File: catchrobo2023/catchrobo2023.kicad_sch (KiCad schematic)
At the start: 35 parts, among them J1 Conn_01x02_Male, J2 Conn_01x02_Male, J3 Conn_01x02_Male, J4 Conn_01x02_Male, J5 Conn_01x02_Male, J6 Conn_01x02_Male, J7 Conn_01x03_Male, J8 Conn_01x03_Male, J9 Conn_01x03_Male, Q1 AO3401A, SW1 SW_SPDT, SW2 SW_DIP_x04, U1 RaspberryPiPicoW, U2 AZ1084-5.0, U3 LBR-127HLD, U4 LBR-127HLD, U5 LBR-127HLD, U6 LBR-127HLD, U7 CD4051BM96, U8 SPT15

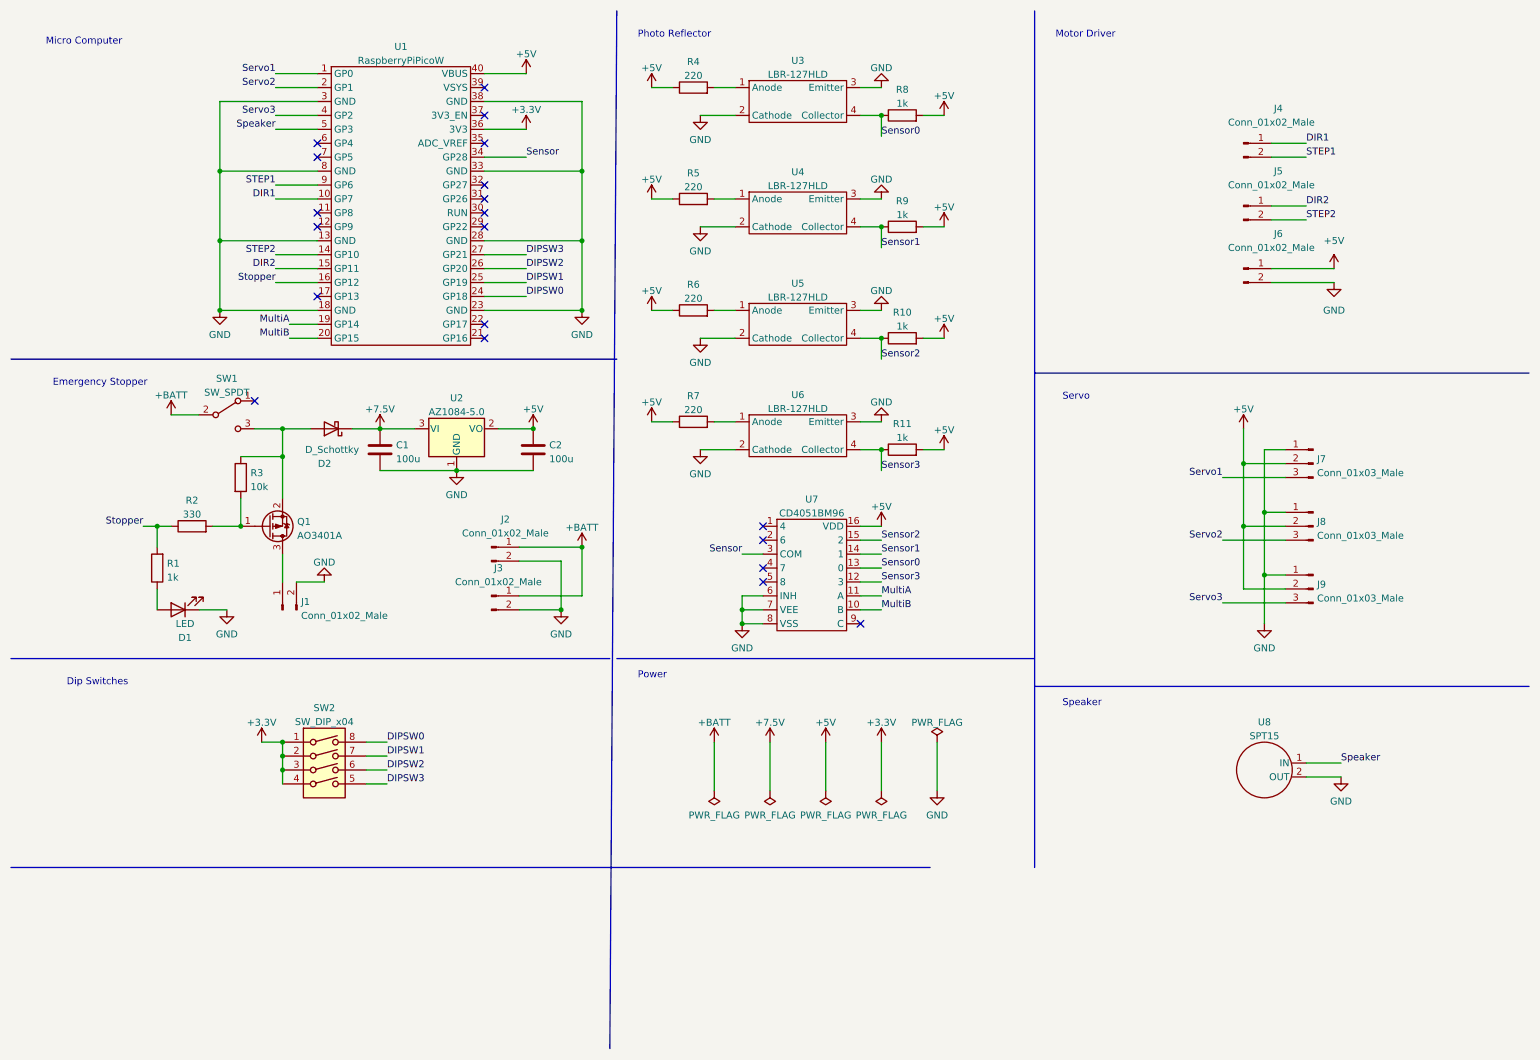
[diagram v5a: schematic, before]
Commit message: コントローラへの配線以外は完了
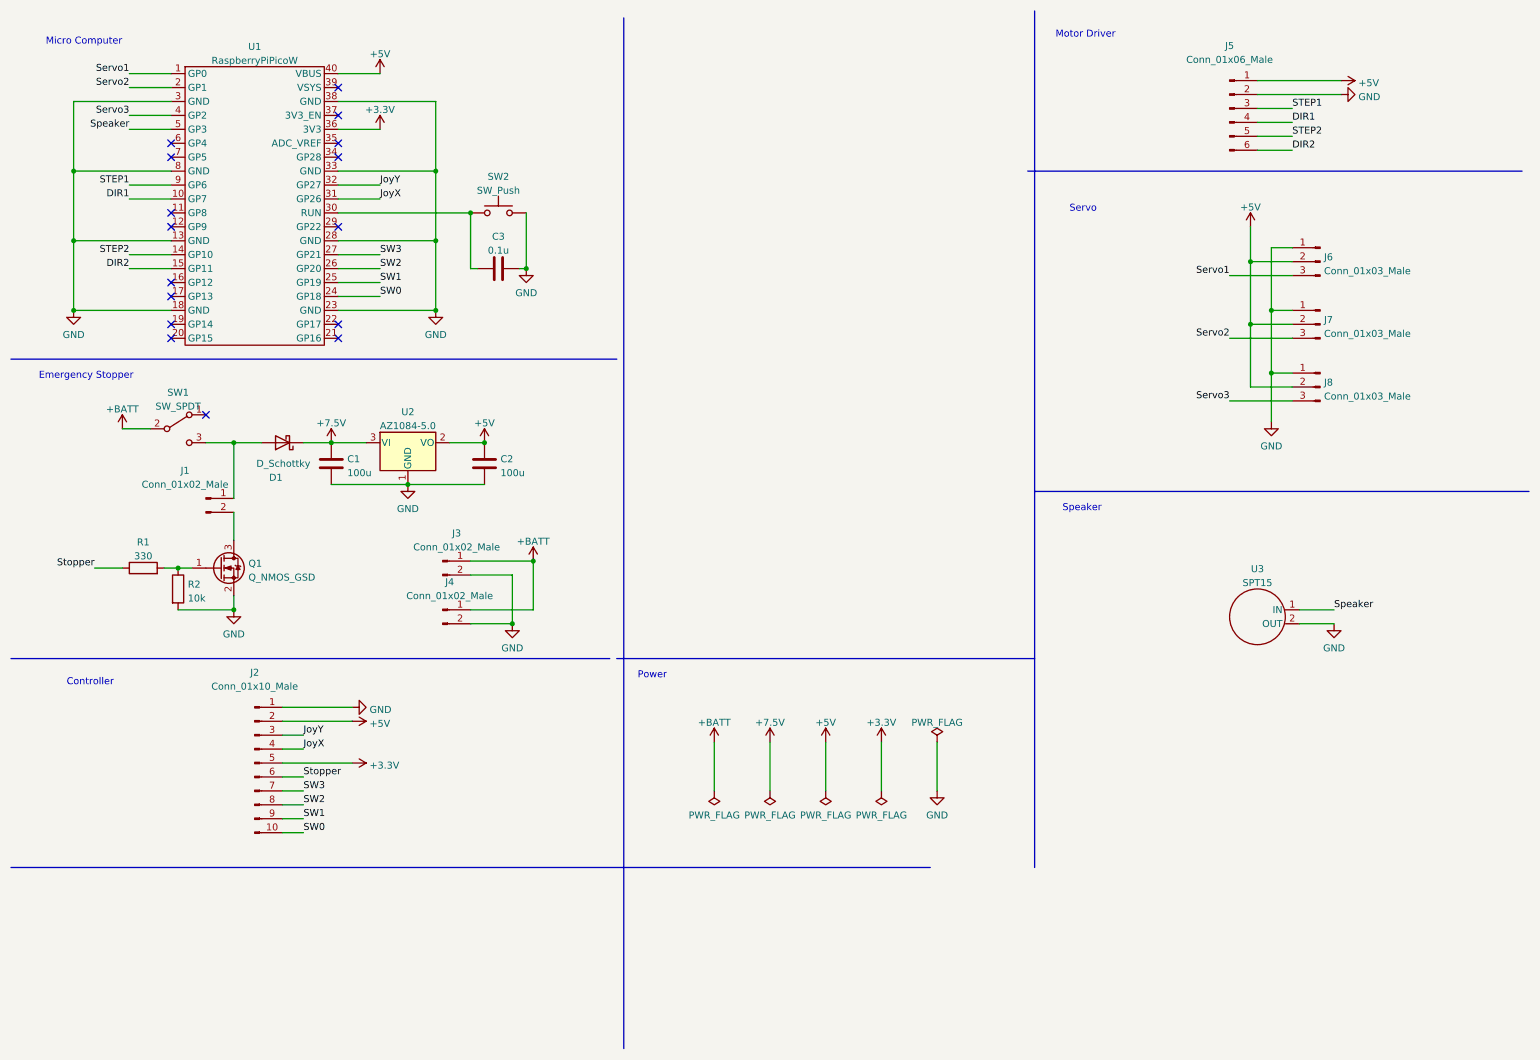
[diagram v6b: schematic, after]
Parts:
- removed D1: LED, LED_THT:LED_D5.0mm, symbol Device:LED
- removed J4, J5, J6: Conn_01x02_Male, Connector_JST:JST_XH_B2B-XH-AM_1x02_P2.50mm_Vertical, symbol Connector:Conn_01x02_Male
- removed Q1: AO3401A, Package_TO_SOT_SMD:SOT-23, symbol Transistor_FET:AO3401A
- removed R10, R11, R8, R9: 1k, Resistor_SMD:R_0402_1005Metric, symbol Device:R
- removed R3: 10k, Resistor_SMD:R_0603_1608Metric, symbol Device:R
- removed R4, R5, R6, R7: 220, Resistor_SMD:R_0603_1608Metric, symbol Device:R
- removed SW2: SW_DIP_x04, Package_DIP:DIP-8_W7.62mm, symbol Switch:SW_DIP_x04
- removed U3, U4, U5, U6: LBR-127HLD, Connector_PinHeader_2.54mm:PinHeader_1x04_P2.54mm_Vertical, symbol catchrobo_parts:LBR-127HLD
- removed U7: CD4051BM96, Catchrobo_parts:SOIC-16-150mil, symbol catchrobo_parts:CD4051BM96
- added C3: 0.1u, Capacitor_SMD:C_0603_1608Metric, symbol Device:C
- added J2: Conn_01x10_Male, Connector_JST:JST_XH_S10B-XH-A_1x10_P2.50mm_Horizontal, symbol Connector:Conn_01x10_Male
- added J5: Conn_01x06_Male, Connector_JST:JST_XH_S6B-XH-A_1x06_P2.50mm_Horizontal, symbol Connector:Conn_01x06_Male
- added Q1: Q_NMOS_GSD, Package_TO_SOT_SMD:SOT-23, symbol Device:Q_NMOS_GSD
- added SW2: SW_Push, Catchrobo_parts:TactSwitch, symbol Switch:SW_Push
- J3: renamed from J2; footprint Connector_JST:JST_XH_B2B-XH-AM_1x02_P2.50mm_Vertical -> Connector_JST:JST_XH_S2B-XH-A_1x02_P2.50mm_Horizontal
- J4: renamed from J3; footprint Connector_JST:JST_XH_B2B-XH-AM_1x02_P2.50mm_Vertical -> Connector_JST:JST_XH_S2B-XH-A_1x02_P2.50mm_Horizontal
- R1: value 1k -> 330; footprint Resistor_SMD:R_0402_1005Metric -> Resistor_SMD:R_0603_1608Metric; LCSC (none) -> C23138
- R2: value 330 -> 10k; LCSC C23138 -> C25804
- U3: renamed from U8; footprint Connector_JST:JST_XH_B2B-XH-AM_1x02_P2.50mm_Vertical -> Catchrobo_parts:PKM13EPYH4000-A0
- renumbered D2 to D1, J7 to J6, J8 to J7, J9 to J8
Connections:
- net +3.3V: now also J2.5 (Pin_5)
- net +5V: now also J2.2 (Pin_2), J5.1 (Pin_1)
- net DIR1: now also J5.4 (Pin_4)
- net DIR2: now also J5.6 (Pin_6)
- net GND: now also R2.2, C3.2, J2.1 (Pin_1), J5.2 (Pin_2), Q1.2 (S), SW2.2; no longer J1.2 (Pin_2)
- net STEP1: now also J5.3 (Pin_3)
- net STEP2: now also J5.5 (Pin_5)
- net Stopper: now also R1.1, J2.6 (Pin_6); no longer R1.2, R2.1, U1.16 (GP12)
- net at J1.1 (Pin_1): now also D1.2 (A), SW1.3 (C)
- net at U1.30 (RUN): now also C3.1, SW2.1
- net JoyX: now reaches U1.31 (GP26)
- net JoyX: now also J2.4 (Pin_4)
- net JoyY: now reaches U1.32 (GP27)
- net JoyY: now also J2.3 (Pin_3)
- net DIPSW0 renamed SW0
- net SW0: now also J2.10 (Pin_10)
- net DIPSW1 renamed SW1
- net SW1: now also J2.9 (Pin_9)
- net DIPSW2 renamed SW2
- net SW2: now also J2.8 (Pin_8)
- net DIPSW3 renamed SW3
- net SW3: now also J2.7 (Pin_7)
- net MultiA: no longer names the net of U1.19 (GP14)
- net MultiB: no longer names the net of U1.20 (GP15)
- net Sensor: no longer names the net of U1.34 (GP28)
- new net: Q1.1 (G), R1.2, R2.1
- new net: J1.2 (Pin_2), Q1.3 (D)
- no-connect marks 20 -> 16
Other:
- note added: "Controller"
- note removed: "Dip Switches"
- note removed: "Photo Reflector"
- moved on the sheet: C1, C2, D1, J1, J3, J4, J6, J7, J8, SW1, U1, U2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

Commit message: pchFetによる電源スイッチを追加
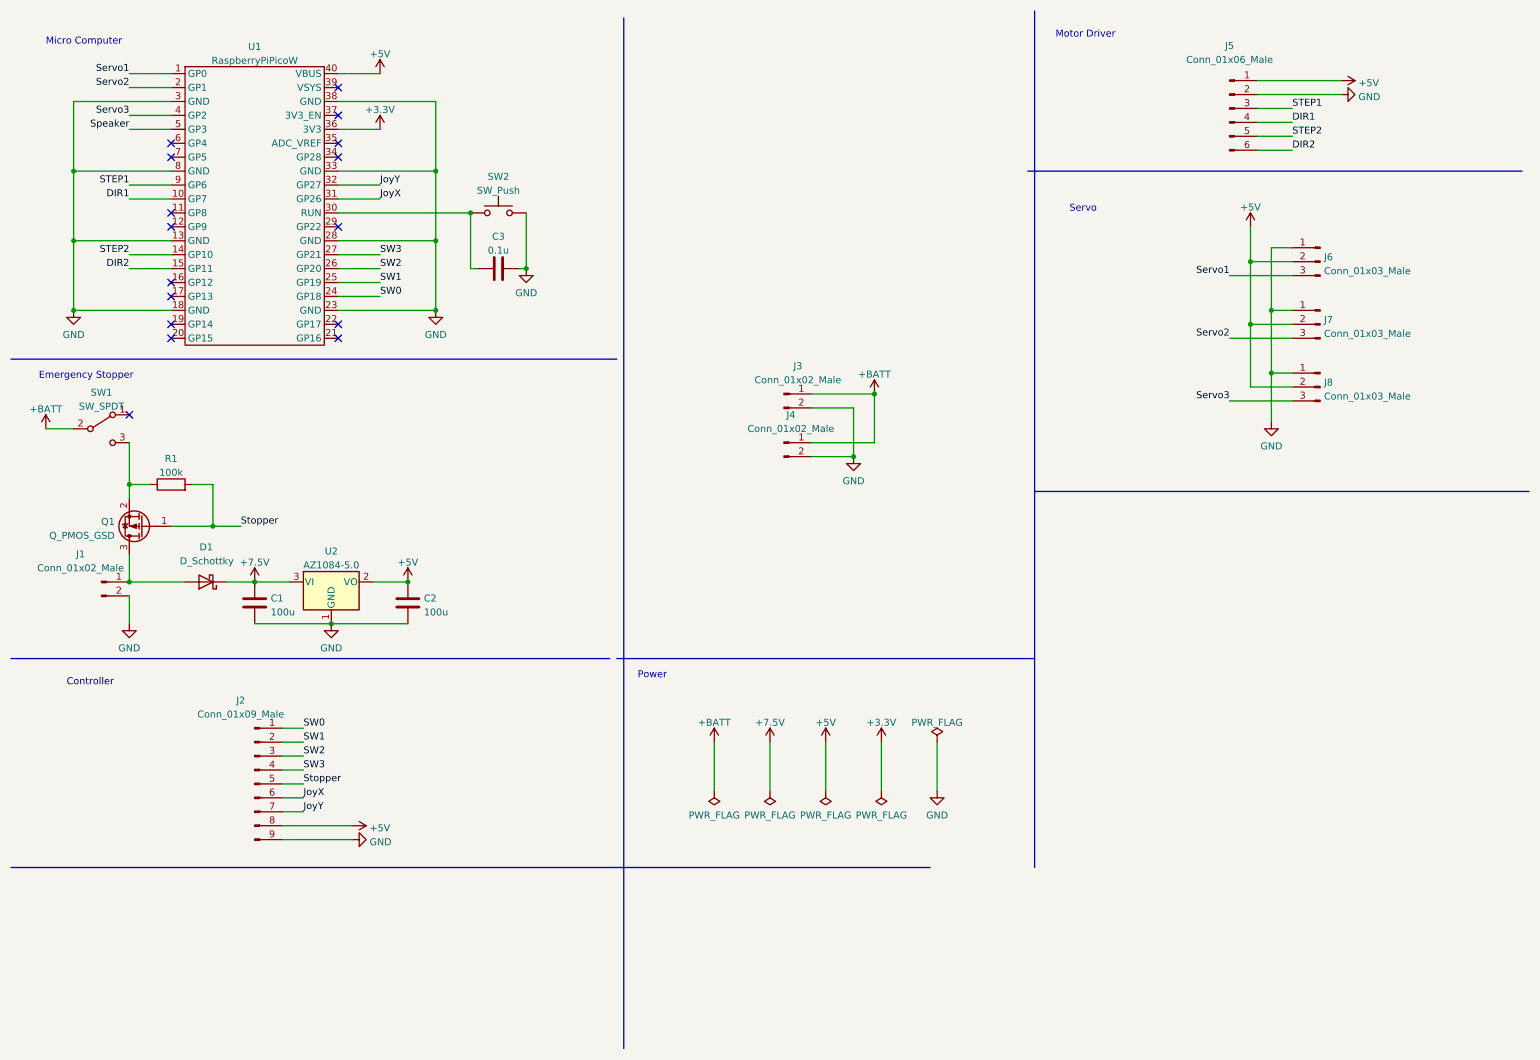
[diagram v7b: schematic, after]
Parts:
- removed J2: Conn_01x10_Male, Connector_JST:JST_XH_S10B-XH-A_1x10_P2.50mm_Horizontal, symbol Connector:Conn_01x10_Male
- removed Q1: Q_NMOS_GSD, Package_TO_SOT_SMD:SOT-23, symbol Device:Q_NMOS_GSD
- removed R2: 10k, Resistor_SMD:R_0603_1608Metric, symbol Device:R
- removed U3: SPT15, Catchrobo_parts:PKM13EPYH4000-A0, symbol catchrobo_parts:SPT15
- added J2: Conn_01x09_Male, Connector_JST:JST_XH_S9B-XH-A-1_1x09_P2.50mm_Horizontal, symbol Connector:Conn_01x09_Male
- added Q1: Q_PMOS_GSD, Package_TO_SOT_SMD:SOT-23, symbol Device:Q_PMOS_GSD
- J1: footprint Connector_JST:JST_XH_B2B-XH-AM_1x02_P2.50mm_Vertical -> Connector_JST:JST_XH_B2B-XH-A_1x02_P2.50mm_Vertical
- R1: value 330 -> 100k; LCSC C23138 -> C25803
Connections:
- net +5V: now also J2.8 (Pin_8)
- net GND: now also J1.2 (Pin_2), J2.9 (Pin_9)
- net JoyX: now also J2.6 (Pin_6)
- net JoyY: now also J2.7 (Pin_7)
- net SW0: now also J2.1 (Pin_1)
- net SW1: now also J2.2 (Pin_2)
- net SW2: now also J2.3 (Pin_3)
- net SW3: now also J2.4 (Pin_4)
- net Stopper: now also R1.2, J2.5 (Pin_5), Q1.1 (G); no longer R1.1
- net at D1.2 (A), J1.1 (Pin_1): now also Q1.3 (D); no longer SW1.3 (C)
- new net: Q1.2 (S), R1.1, SW1.3 (C)
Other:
- note removed: "Speaker"
- moved on the sheet: C1, C2, D1, J1, J3, J4, SW1, U2

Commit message: 回収機基板設計完了
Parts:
- removed SW1: SW_SPDT, Catchrobo_parts:2MS1-T1-B4-M2-Q-E-S, symbol Switch:SW_SPDT
- J1: footprint Connector_JST:JST_XH_B2B-XH-A_1x02_P2.50mm_Vertical -> Connector_JST:JST_XH_S2B-XH-A_1x02_P2.50mm_Horizontal
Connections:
- net +BATT: now also Q1.2 (S), R1.1
- no-connect marks 16 -> 15
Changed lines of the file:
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@@
   (no_connect (at 69.85 69.85))
   (no_connect (at 69.85 36.83))
-  (no_connect (at 31.75 83.82))
   (no_connect (at 69.85 34.29))
   (no_connect (at 69.85 29.21))
@@
   )
   (wire (pts (xy 54.61 114.3) (xy 60.96 114.3))
-    (stroke (width 0) (type default) (color 0 0 0 0))
-  )
-  (wire (pts (xy 16.51 86.36) (xy 21.59 86.36))
     (stroke (width 0) (type default) (color 0 0 0 0))
   )
@@
     (property "Reference" "J1" (id 0) (at 22.86 109.22 0))
     (property "Value" "Conn_01x02_Male" (id 1) (at 22.86 111.76 0))
-    (property "Footprint" "Connector_JST:JST_XH_B2B-XH-A_1x02_P2.50mm_Vertical" (id 2) (at 26.67 114.3 0)
+    (property "Footprint" "Connector_JST:JST_XH_S2B-XH-A_1x02_P2.50mm_Horizontal" (id 2) (at 26.67 114.3 0)
       (effects (font (size 1.27 1.27)) hide)
     )
@@
     (pin "2")
   )
-  (symbol (lib_id "power:+BATT") (at 16.51 86.36 0) (unit 1)
-    (in_bom yes) (on_board yes) (fields_autoplaced)
-    (property "Reference" "#PWR01" (id 0) (at 16.51 90.17 0)
-      (effects (font (size 1.27 1.27)) hide)
-    )
-    (property "Value" "+BATT" (id 1) (at 16.51 82.7842 0))
-    (property "Footprint" "" (id 2) (at 16.51 86.36 0)
-      (effects (font (size 1.27 1.27)) hide)
-    )
-    (property "Datasheet" "" (id 3) (at 16.51 86.36 0)
+  (symbol (lib_id "power:+BATT") (at 31.75 88.9 0) (unit 1)
+    (in_bom yes) (on_board yes) (fields_autoplaced)
+    (property "Reference" "#PWR01" (id 0) (at 31.75 92.71 0)
+      (effects (font (size 1.27 1.27)) hide)
+    )
+    (property "Value" "+BATT" (id 1) (at 31.75 85.3242 0))
+    (property "Footprint" "" (id 2) (at 31.75 88.9 0)
+      (effects (font (size 1.27 1.27)) hide)
+    )
+    (property "Datasheet" "" (id 3) (at 31.75 88.9 0)
       (effects (font (size 1.27 1.27)) hide)
     )
@@
     (pin "3")
   )
-  (symbol (lib_id "Switch:SW_SPDT") (at 26.67 86.36 0) (unit 1)
-    (in_bom yes) (on_board yes) (fields_autoplaced)
-    (property "Reference" "SW1" (id 0) (at 26.67 79.7392 0))
-    (property "Value" "SW_SPDT" (id 1) (at 26.67 82.2761 0))
-    (property "Footprint" "Catchrobo_parts:2MS1-T1-B4-M2-Q-E-S" (id 2) (at 26.67 86.36 0)
-      (effects (font (size 1.27 1.27)) hide)
-    )
-    (property "Datasheet" "~" (id 3) (at 26.67 86.36 0)
-      (effects (font (size 1.27 1.27)) hide)
-    )
-    (pin "1")
-    (pin "2")
-    (pin "3")
-  )
   (symbol (lib_id "power:GND") (at 179.07 152.4 0) (unit 1)
     (in_bom yes) (on_board yes) (fields_autoplaced)
@@
     )
     (path "/6a340abe-3ed6-4077-ba04-0f375d73ed88"
-      (reference "J1") (unit 1) (value "Conn_01x02_Male") (footprint "Connector_JST:JST_XH_B2B-XH-A_1x02_P2.50mm_Vertical")
+      (reference "J1") (unit 1) (value "Conn_01x02_Male") (footprint "Connector_JST:JST_XH_S2B-XH-A_1x02_P2.50mm_Horizontal")
     )
     (path "/9daa5f44-3d7d-483c-bdfb-519fb183b0fd"
@@
       (reference "R1") (unit 1) (value "100k") (footprint "Resistor_SMD:R_0603_1608Metric")
     )
-    (path "/f8c78e15-c342-4ab0-8f4b-67d61e7bd8ef"
-      (reference "SW1") (unit 1) (value "SW_SPDT") (footprint "Catchrobo_parts:2MS1-T1-B4-M2-Q-E-S")
-    )
     (path "/2fcba6da-3043-4796-9931-23d1f03cba42"
